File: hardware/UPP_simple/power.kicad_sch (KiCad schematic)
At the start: 14 parts, among them J2 Conn_01x02, U4 MC78M12CDTG, U5 LM1117IMP-5.0, U6 MCP1700x-330xxMB

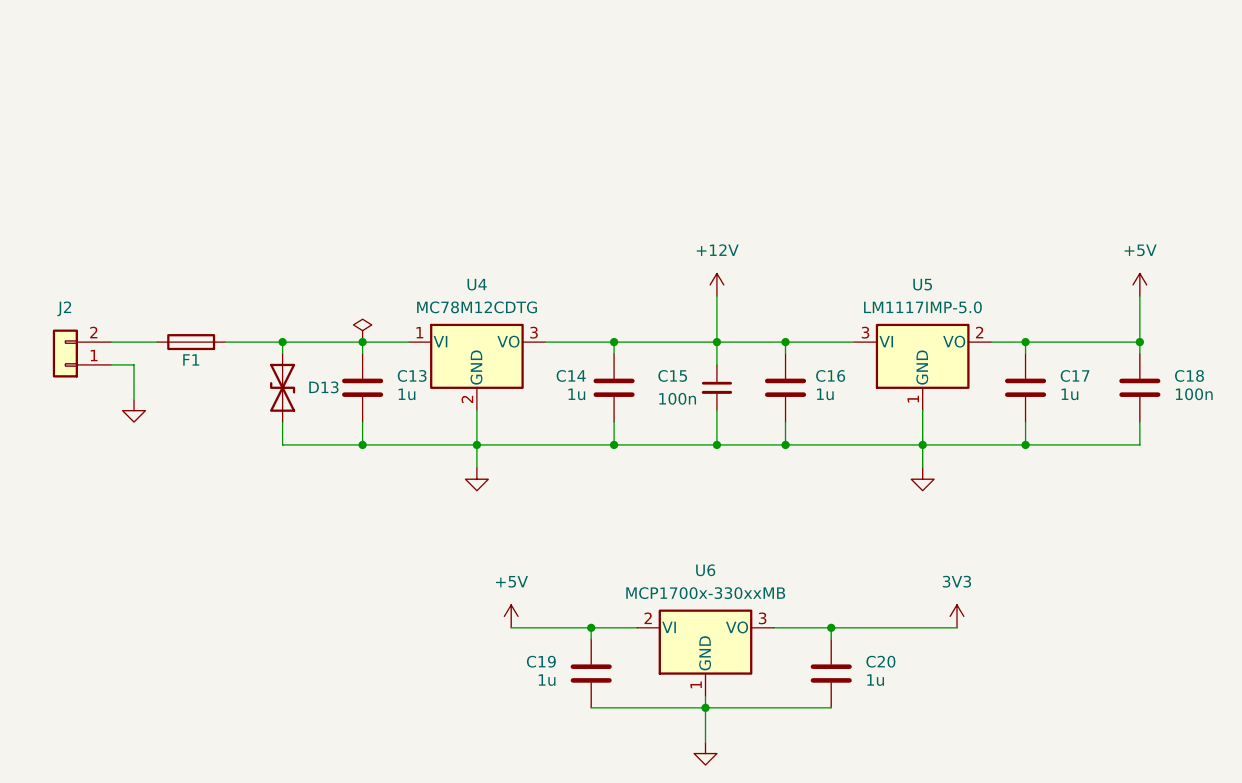
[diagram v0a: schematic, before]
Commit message: Changed Opamps cleared schematic
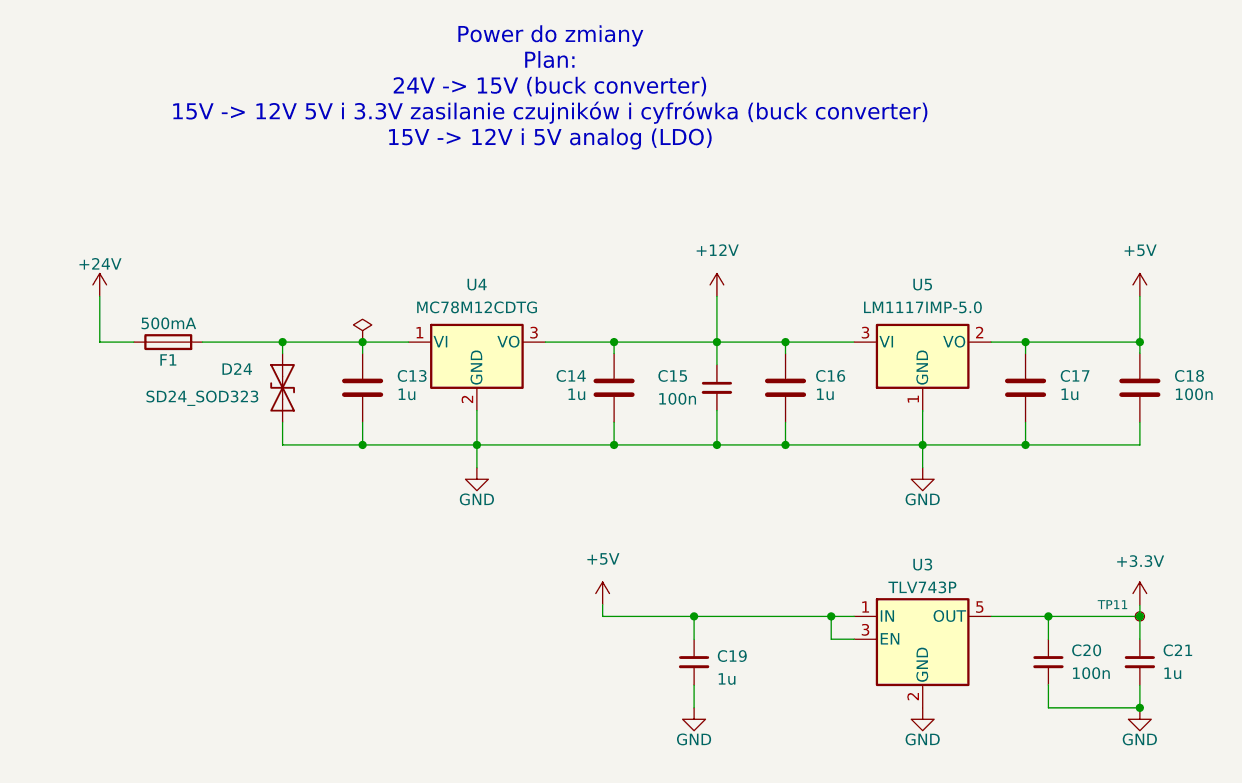
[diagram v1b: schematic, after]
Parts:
- removed C19, C20: 1u, Capacitor_SMD:C_0603_1608Metric_Pad1.08x0.95mm_HandSolder, symbol Device:C
- removed D13: LBD52A24L01, Diode_SMD:D_SOD-523, symbol Diode:1N630xCA
- removed J2: Conn_01x02, symbol Connector_Generic:Conn_01x02
- removed U6: MCP1700x-330xxMB, Package_TO_SOT_SMD:SOT-89-3, symbol Regulator_Linear:MCP1700x-330xxMB
- added C19, C21: 1u, Capacitor_SMD:C_0603_1608Metric, symbol Device:C_Small
- added C20: 100n, Capacitor_SMD:C_0603_1608Metric, symbol Device:C_Small
- added D24: SD24_SOD323, Diode_SMD:D_SOD-323, symbol Diode:SD24_SOD323
- added TP11: TestPoint_Small, TestPoint:TestPoint_Pad_D1.0mm, symbol Connector:TestPoint_Small
- added U3: TLV743P, Package_TO_SOT_SMD:SOT-23-5, symbol Regulator_Linear:TLV73330PDBV
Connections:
- net +5V: now also C19.1, U3.1 (IN), U3.3 (EN)
- net GND: now also C19.2, C20.2, C21.2, D24.1 (A1), U3.2 (GND)
- net at C13.1, F1.2, U4.1 (VI): now also D24.2 (A2)
- net +24V: now reaches F1.1
- new net +3.3V: C20.1, C21.1, TP11.1, U3.5 (OUT)
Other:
- note added: "Power do zmiany Plan: 24V -> 15V (buck converter) 15V -> 12V 5V i 3.3V zasilanie czujników i cyfrówka (buck converter) 15V -> 12V i 5V analog (LDO)"
- title: Universal use measuring PCB -> Universal Measurement Board
- moved on the sheet: F1
